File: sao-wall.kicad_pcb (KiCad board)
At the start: 2 copper layers, 60 x 52 mm, 28 parts, among them J1 Conn_02x03_Odd_Even, J2 Conn_02x03_Odd_Even, J3 Conn_02x03_Odd_Even, J4 Conn_02x03_Odd_Even, J5 Conn_02x03_Odd_Even, J6 Conn_02x03_Odd_Even, J7 Conn_Up, J8 Conn_Down, U1 LM2594M-3.3, U2 LM2594M-3.3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

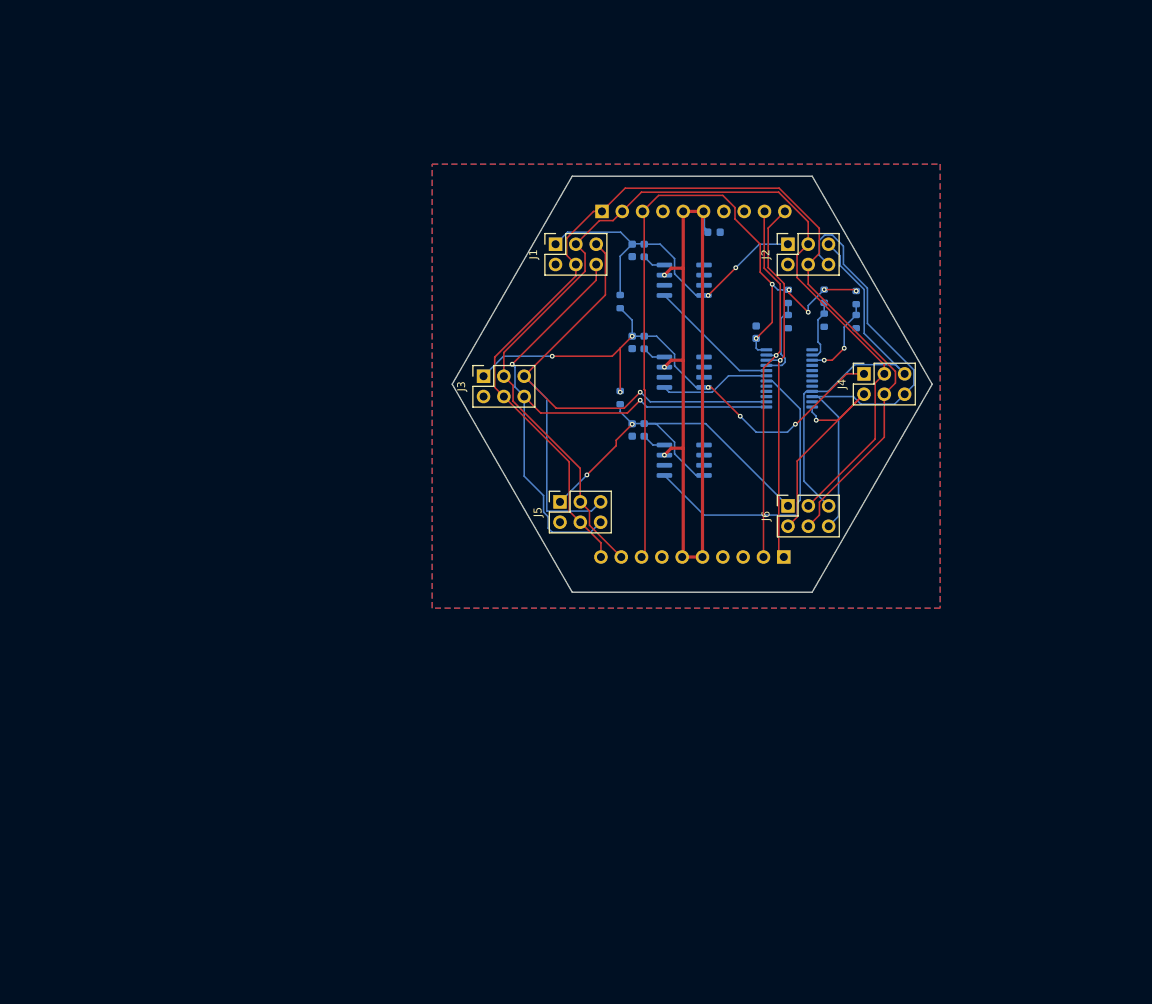
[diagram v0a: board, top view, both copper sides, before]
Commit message: Make tile larger, still needs routing
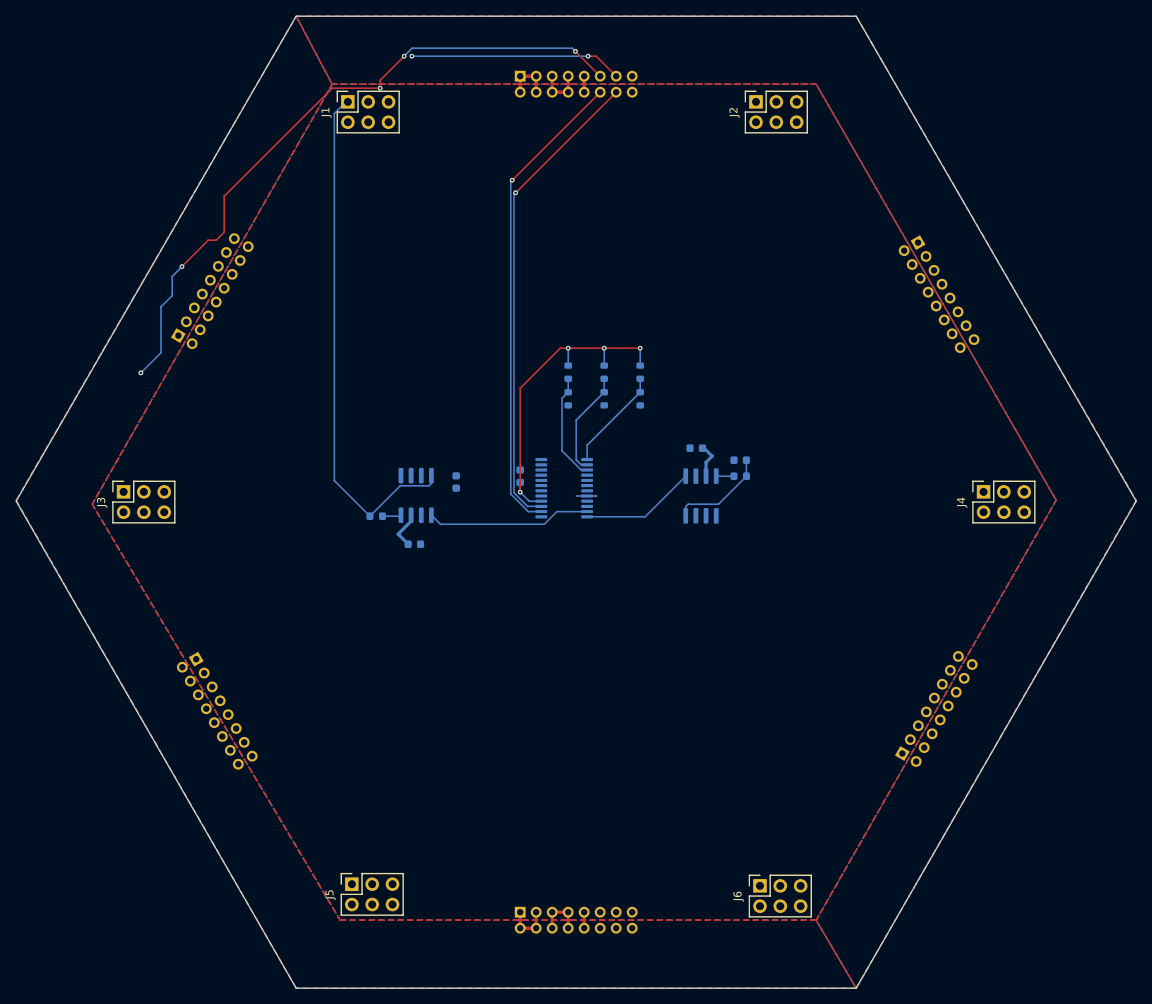
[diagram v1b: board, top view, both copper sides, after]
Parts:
- removed L3: L, Inductor_SMD:L_0603_1608Metric
- removed R1, R2: R, Resistor_SMD:R_0603_1608Metric
- removed U3: LM2594M-3.3, Package_SO:SOIC-8_3.9x4.9mm_P1.27mm
- added J10: Conn_02x08_Odd_Even, Connector_PinHeader_2.00mm:PinHeader_2x08_P2.00mm_Vertical, B.Cu at (93.5, 142.0)
- added J11: Conn_02x08_Odd_Even, Connector_PinHeader_2.00mm:PinHeader_2x08_P2.00mm_Vertical, B.Cu at (53.0, 110.4)
- added J12: Conn_02x08_Odd_Even, Connector_PinHeader_2.00mm:PinHeader_2x08_P2.00mm_Vertical, B.Cu at (50.8, 69.9)
- added J9: Conn_02x08_Odd_Even, Connector_PinHeader_2.00mm:PinHeader_2x08_P2.00mm_Vertical, B.Cu at (141.3, 122.2)
- J7: value Conn_Up -> Conn_02x08_Odd_Even; footprint Connector_PinSocket_2.54mm:PinSocket_1x10_P2.54mm_Horizontal -> Connector_PinHeader_2.00mm:PinHeader_2x08_P2.00mm_Vertical
- J8: value Conn_Down -> Conn_02x08_Odd_Even; footprint Connector_PinSocket_2.54mm:PinSocket_1x10_P2.54mm_Horizontal -> Connector_PinHeader_2.00mm:PinHeader_2x08_P2.00mm_Vertical
- moved J5 54.4 mm to (72.5, 138.5)
- moved J6 47.6 mm to (123.5, 138.7)
- moved J3 47.3 mm to (43.9, 89.5)
- moved L1 47.2 mm to (75.5, 92.5), turned to 180 degrees
- moved U1 43.0 mm to (80.5, 89.9), turned to -90 degrees
- moved J8 42.7 mm to (143.2, 58.3), turned to -150 degrees
- moved C1 36.4 mm to (85.5, 88.2)
- moved C4 34.6 mm to (93.5, 87.5)
- moved J1 31.5 mm to (72.0, 40.7)
- moved U4 31.3 mm to (99.0, 89.0)
- moved C3 30.7 mm to (80.3, 96.0), turned to 0 degrees
- moved R6 29.2 mm to (104.0, 77.8)
- moved R4 29.1 mm to (99.5, 77.8)
- moved R5 29.1 mm to (104.0, 74.5)
- moved R3 29.1 mm to (99.5, 74.5)
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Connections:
- C1 pad 1: VCC-A -> VCC-LEFT
- C2 pad 1: VCC-B -> VCC-RIGHT
- C3 pad 1: VCC-C -> +5V
- J1 pad 1: VCC-A -> VCC-LEFT
- J1 pad 3: /SDA1 -> /SAO_SDA
- J1 pad 4: /SCL1 -> /SAO_SCL
- J1 pad 5: /GPIO1L -> /TOP_GPIO1
- J1 pad 6: /GPIO2L -> /TOP_GPIO2
- J2 pad 1: VCC-A -> VCC-RIGHT
- J2 pad 3: /SDA1 -> /SAO_SDA
- J2 pad 4: /SCL1 -> /SAO_SCL
- J2 pad 5: /GPIO1R -> /TOP_GPIO1
- J2 pad 6: /GPIO2R -> /TOP_GPIO2
- J3 pad 1: VCC-B -> VCC-LEFT
- J3 pad 3: /SDA1 -> /SAO_SDA
- J3 pad 4: /SCL1 -> /SAO_SCL
- J3 pad 5: /GPIO1L -> /MID_GPIO1
- J3 pad 6: /GPIO2L -> /MID_GPIO2
- J4 pad 1: VCC-B -> VCC-RIGHT
- J4 pad 3: /SDA1 -> /SAO_SDA
- J4 pad 4: /SCL1 -> /SAO_SCL
- J4 pad 5: /GPIO1R -> /MID_GPIO1
- J4 pad 6: /GPIO2R -> /MID_GPIO2
- J5 pad 1: VCC-C -> VCC-LEFT
- J5 pad 3: /SDA1 -> /SAO_SDA
- J5 pad 4: /SCL1 -> /SAO_SCL
- J5 pad 5: /GPIO1L -> /BOT_GPIO1
- J5 pad 6: /GPIO2L -> /BOT_GPIO2
- J6 pad 1: VCC-C -> VCC-RIGHT
- J6 pad 3: /SDA1 -> /SAO_SDA
- J6 pad 4: /SCL1 -> /SAO_SCL
- J6 pad 5: /GPIO1R -> /BOT_GPIO1
- J6 pad 6: /GPIO2R -> /BOT_GPIO2
- J7 pad 1: /SCL1 -> GND
- J7 pad 10: /SCL2 -> +3.3V
- J7 pad 2: /SDA1 -> GND
- J7 pad 3: +3.3V -> GND
- J7 pad 7: GND -> +5V
- J7 pad 8: unconnected-(J7-Pin_8-Pad8) -> +5V
- J7 pad 9: /SDA2 -> +3.3V
- J8 pad 1: /SCL2 -> GND
- J8 pad 10: /SCL1 -> +3.3V
- J8 pad 2: /SDA2 -> GND
- J8 pad 3: unconnected-(J8-Pin_3-Pad3) -> GND
- J8 pad 7: GND -> +5V
- J8 pad 8: +3.3V -> +5V
- J8 pad 9: /SDA1 -> +3.3V
- L1 pad 2: VCC-A -> VCC-LEFT
- L2 pad 2: VCC-B -> VCC-RIGHT
- U1 pad 4: VCC-A -> VCC-LEFT
- U1 pad 5: /EN-A -> /EN-LEFT
- U2 pad 4: VCC-B -> VCC-RIGHT
- U2 pad 5: /EN-B -> /EN-RIGHT
- U4 pad 1: unconnected-(U4-~{INT}-Pad1) -> /A2
- U4 pad 10: /GPIO2R -> /BOT_GPIO2
- U4 pad 11: unconnected-(U4-P07-Pad11) -> /EN-LEFT
- U4 pad 12: GND -> /EN-RIGHT
- U4 pad 13: /GPIO2L -> unconnected-(U4-~{INT}-Pad13)
- U4 pad 14: /GPIO1L -> /CTL_SCL
- U4 pad 15: unconnected-(U4-P12-Pad15) -> /CTL_SDA
- U4 pad 16: unconnected-(U4-P13-Pad16) -> +3.3V
- U4 pad 17: unconnected-(U4-P14-Pad17) -> (no net)
- U4 pad 18: /EN-C -> (no net)
- U4 pad 19: /EN-B -> (no net)
- U4 pad 20: /EN-A -> (no net)
- U4 pad 21: /A0 -> (no net)
- U4 pad 22: /SCL2 -> (no net)
- U4 pad 23: /SDA2 -> (no net)
- U4 pad 24: +3.3V -> (no net)
- U4 pad 3: /A2 -> /A0
- U4 pad 4: unconnected-(U4-P00-Pad4) -> /TOP_GPIO1
- U4 pad 5: unconnected-(U4-P01-Pad5) -> /TOP_GPIO2
- U4 pad 6: unconnected-(U4-P02-Pad6) -> /MID_GPIO1
- U4 pad 7: unconnected-(U4-P03-Pad7) -> /MID_GPIO2
- U4 pad 8: unconnected-(U4-P04-Pad8) -> GND
- U4 pad 9: /GPIO1R -> /BOT_GPIO1
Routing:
- net /SCL1: track 133.1 -> 0.00 mm
- net /SDA1: track 128.2 -> 0.00 mm
- net /SAO_SCL: track 0.00 -> 83.7 mm, vias 0 -> 5
- net +5V: track 102.5 -> 20.3 mm, vias 3 -> 0
- net /GPIO1L: track 79.4 -> 0.00 mm, vias 1 -> 0
- net /GPIO2L: track 78.4 -> 0.00 mm, vias 2 -> 0
- net VCC-B: track 67.7 -> 0.00 mm, vias 6 -> 0
- net VCC-LEFT: track 0.00 -> 64.2 mm
- net /GPIO2R: track 61.0 -> 0.00 mm
- net /CTL_SCL: track 0.00 -> 59.6 mm, vias 0 -> 1
- net /CTL_SDA: track 0.00 -> 59.5 mm, vias 0 -> 1
- net VCC-C: track 51.1 -> 0.00 mm, vias 2 -> 0
- net /GPIO1R: track 50.0 -> 0.00 mm
- net +3.3V: track 93.2 -> 44.9 mm, vias 6 -> 4
- net /SCL2: track 47.2 -> 0.00 mm, vias 1 -> 0
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- added copper zone on B.Cu, net +3.3V
- added copper zone on F.Cu, net +5V
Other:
- board size 60 x 52 mm -> 140 x 121.5 mm

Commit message: Routed traces
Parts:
- moved C1 10.3 mm to (75.5, 90.5), turned to 0 degrees
- moved C4 8.20 mm to (98.5, 94.0), turned to 0 degrees
- moved C2 4.00 mm to (121.0, 89.5)
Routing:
- net /SAO_SDA: track 26.6 -> 383.1 mm, vias 2 -> 19
- net /SAO_SCL: track 83.7 -> 402.3 mm, vias 5 -> 20
- net /CTL_SCL: track 59.6 -> 321.4 mm, vias 1 -> 11
- net /CTL_SDA: track 59.5 -> 309.6 mm, vias 1 -> 13
- net VCC-RIGHT: track 12.1 -> 143.6 mm, vias 0 -> 4
- net /MID_GPIO1: track 0.00 -> 122.8 mm, vias 0 -> 5
- net /MID_GPIO2: track 0.00 -> 120.2 mm, vias 0 -> 3
- net /BOT_GPIO2: track 0.00 -> 108.5 mm, vias 0 -> 5
- net /BOT_GPIO1: track 0.00 -> 107.6 mm, vias 0 -> 5
- net /TOP_GPIO1: track 0.00 -> 105.4 mm, vias 0 -> 3
- net /TOP_GPIO2: track 0.00 -> 103.6 mm, vias 0 -> 3
- net +5V: track 20.3 -> 112.1 mm, vias 0 -> 2
- net VCC-LEFT: track 64.2 -> 145.6 mm, vias 0 -> 3
- net +3.3V: track 44.9 -> 106.3 mm, vias 4 -> 5
- net GND: track 14.5 -> 40.9 mm
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
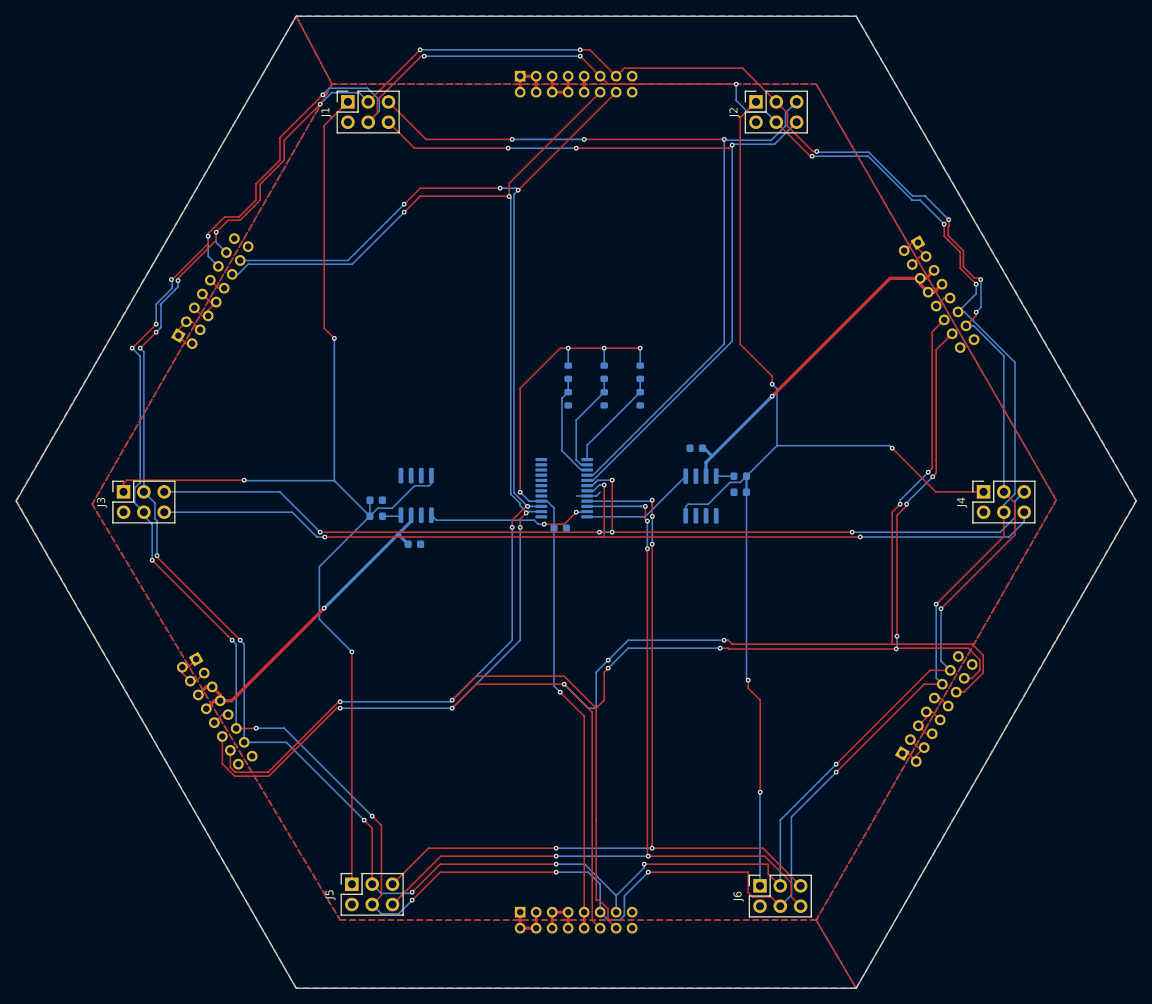
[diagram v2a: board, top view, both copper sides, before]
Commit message: Small adjustments for pours
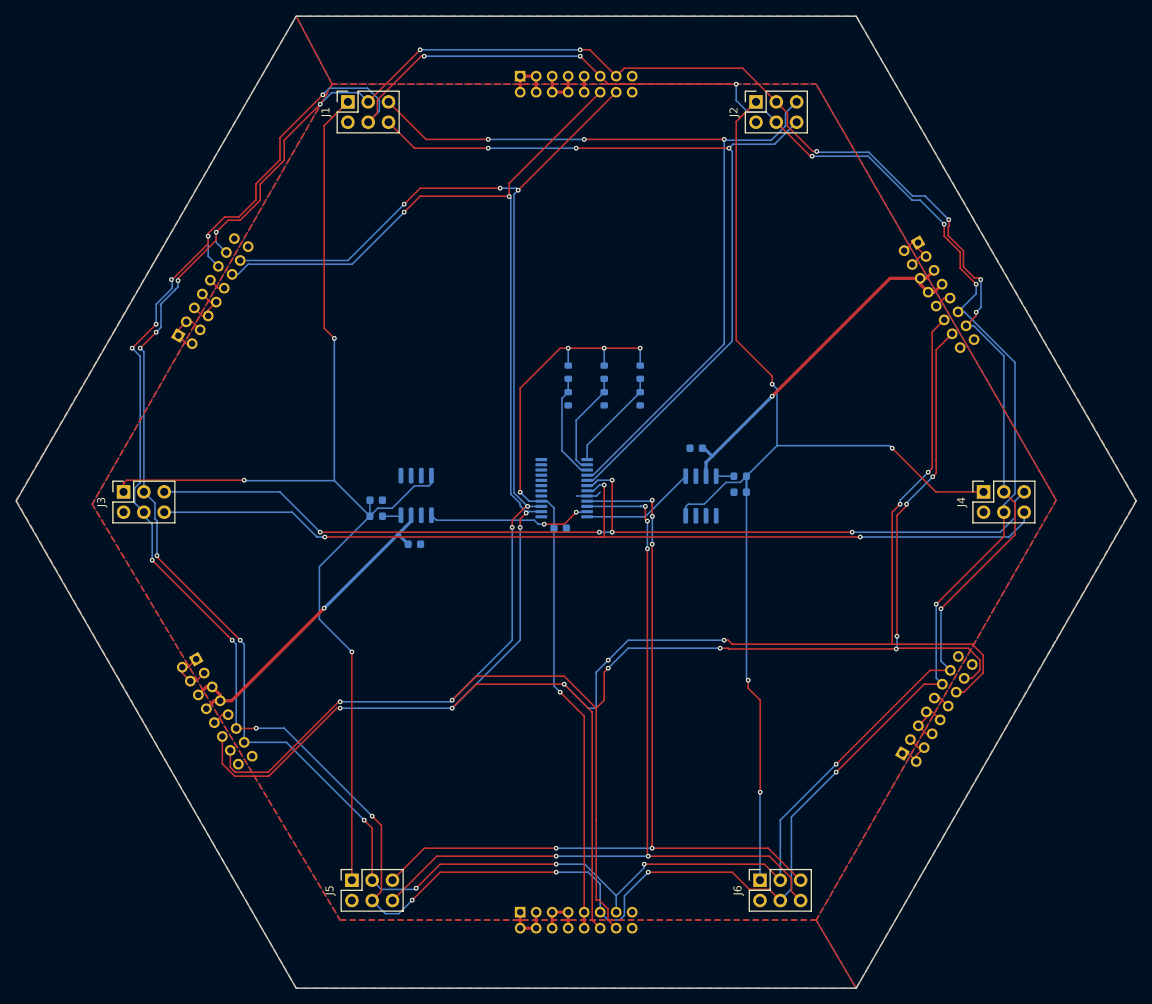
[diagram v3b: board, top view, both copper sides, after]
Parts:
- moved J6 0.71 mm to (123.5, 138.0)
- moved J5 0.50 mm to (72.5, 138.0)
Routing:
- net /SAO_SCL: track 402.3 -> 400.3 mm
- net /SAO_SDA: track 383.1 -> 382.1 mm
- net /BOT_GPIO2: track 108.5 -> 107.9 mm
- net VCC-LEFT: track 145.6 -> 145.1 mm
